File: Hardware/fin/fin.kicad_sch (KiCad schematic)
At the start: 0 parts

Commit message: move over old schematic
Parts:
- added C1, C3, C5: 10 nF, Capacitor_SMD:C_0603_1608Metric, symbol Device:C_Small
- added C10, C4: 1 uF, Capacitor_SMD:C_0603_1608Metric, symbol Device:C_Small
- added C11: 220 nF, Capacitor_SMD:C_0603_1608Metric, symbol Device:C_Small
- added C12, C13, C2, C6, C7, C8, C9: 100nF, Capacitor_SMD:C_0603_1608Metric, symbol Device:C_Small
- added D1, D2, D3, D4: LED, LED_SMD:LED_0603_1608Metric, symbol Device:LED
- added D5: DFLS160-7, Diode_SMD:D_PowerDI-123, symbol Device:D_Small
- added H1, H2, H3, H4: MountingHole_Pad, MountingHole:MountingHole_2.2mm_M2_Pad, symbol Mechanical:MountingHole_Pad
- added J1: USB_C_Receptacle_USB2.0_16P, Connector_USB:USB_C_Receptacle_GCT_USB4105-xx-A_16P_TopMnt_Horizontal, symbol Connector:USB_C_Receptacle_USB2.0_16P
- added J10, J11, J12, J13, J14, J15, J16, J17, J18, J6, J7, J8, J9: Conn_01x01_Pin, FinLib:SimpleThroughHole, symbol Connector:Conn_01x01_Pin
- added J2, J3: Conn_01x04_Pin, Connector_PinHeader_2.54mm:PinHeader_1x04_P2.54mm_Vertical, symbol Connector:Conn_01x04_Pin
- added J4: Conn_01x08_Pin, Connector_PinHeader_2.54mm:PinHeader_1x08_P2.54mm_Vertical, symbol Connector:Conn_01x08_Pin
- added J5: Conn_01x04_Pin, FinLib:FlexCable, symbol Connector:Conn_01x04_Pin
- added R1: 10 k, Resistor_SMD:R_0603_1608Metric, symbol Device:R_US
- added R10, R7, R8, R9: 220, Resistor_SMD:R_0603_1608Metric, symbol Device:R_Small_US
- added R11, R12, R13, R14: 1 k, Resistor_SMD:R_0603_1608Metric, symbol Device:R_US
- added R15, R16: 5.1k, Resistor_SMD:R_0603_1608Metric, symbol Device:R_Small_US
- added R2: 5K, Resistor_SMD:R_0603_1608Metric, symbol Device:R_Small_US
- added R3, R4, R5, R6: 2.5 k, Resistor_SMD:R_0603_1608Metric, symbol Device:R_US
- added SW1, SW2: SW_Push, FinLib:SW_FSM2JMTR_TEC, symbol Switch:SW_Push
- added TP1, TP2, TP3, TP4: TestPoint, Connector_PinHeader_2.54mm:PinHeader_1x01_P2.54mm_Vertical, symbol Connector:TestPoint
- added TP10, TP11, TP12, TP13, TP14, TP15, TP16, TP17, TP18, TP19, TP20, TP21, TP22, TP23, TP24, TP25, TP9: TestPoint, FinLib:TestPoint, symbol Connector:TestPoint
- added TP5, TP6, TP7, TP8: TestPoint, Connector_PinSocket_2.54mm:PinSocket_1x01_P2.54mm_Vertical, symbol Connector:TestPoint
- added U1: ADS131M03QPWRQ1, FinLib:ADS131M03, symbol FinLib:ADS131M03QPWRQ1
- added U2: STM32L412C8Tx, Package_QFP:LQFP-48_7x7mm_P0.5mm, symbol MCU_ST_STM32L4:STM32L412C8Tx
- added U3: W25N512GVEIG, FinLib:WSON8_8x6_E_WIN, symbol FinLib:W25N512GVEIG
- added U4: TMP235A4DBZR, FinLib:TMP235A4DBZR, symbol FinLib:TMP235A4DBZR
- added U5: FT232RNQ-REEL, FinLib:QFN32_FT232_FTD, symbol FinLib:FT232RNQ-REEL
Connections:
- new net: D4.1 (K), R10.2
- new net: R2.2, SW2.2, U2.44 (PH3)
- new net: C2.2, SW1.2, U2.7 (NRST)
- new net: D3.1 (K), R9.2
- new net: D5.2 (A), J1.A4 (VBUS), J1.A9 (VBUS), J1.B4 (VBUS), J1.B9 (VBUS)
- new net: D1.1 (K), R7.1
- new net: D2.1 (K), R8.2
- new net: C5.1, R5.2, U1.7 (AIN2P)
- new net: C5.2, R6.1, U1.8 (AIN2N)
- new net: J1.A5 (CC1), R15.1
- new net: C1.1, R1.2, U1.3 (AIN0P)
- new net: C13.1, U5.16 (3V3OUT)
- new net: C3.1, R3.2, U1.5 (AIN1N)
- new net: C3.2, R4.1, U1.6 (AIN1P)
- new net: J1.B5 (CC2), R16.1
- new net: C11.1, U1.18 (CAP)
- new net +3.3V: C10.1, C12.1, C4.2, C6.1, C7.1, C8.1, C9.1, D1.2 (A), D2.2 (A), D3.2 (A), J2.1 (Pin_1), J3.1 (Pin_1), J4.7 (Pin_7), J5.1 (Pin_1), R11.2, R13.1, SW2.1, U1.1 (AVDD), U1.20 (DVDD), U2.1 (VBAT), U2.24 (VDD), U2.48 (VDD), U2.9 (VDDA), U3.8 (VCC), U4.1 (VDD), U5.1 (VCCIO)
- new net +5V: D5.1 (K), U5.19 (VCC)
- new net ADC_~{SYNC}/~{RST}: TP14.1, U1.11 (*SYNC/*RESET), U2.46 (PB9)
- new net AVBAY_SYNC: J5.3 (Pin_3), U2.22 (PB11)
- new net GAUGE1_IN_N: R11.1, R12.1, R5.1
- new net GAUGE1_IN_P: J2.2 (Pin_2), J2.3 (Pin_3), R6.2
- new net GAUGE2_IN_N: R13.2, R14.2, R4.2
- new net GAUGE2_IN_P: J3.2 (Pin_2), J3.3 (Pin_3), R3.1
- new net GND: C1.2, C10.2, C11.2, C12.2, C13.2, C2.1, C4.1, C6.2, C7.2, C8.2, C9.2, H1.1, H2.1, H3.1, H4.1, J1.A1 (GND), J1.A12 (GND), J1.B1 (GND), J1.B12 (GND), J2.4 (Pin_4), J3.4 (Pin_4), J4.8 (Pin_8), J5.4 (Pin_4), R10.1, R12.2, R14.1, R15.2, R16.2, R2.1, R7.2, SW1.1, TP1.1, TP2.1, TP3.1, TP4.1, TP5.1, TP6.1, TP7.1, TP8.1, U1.19 (DGND), U1.2 (AGND), U1.4 (AIN0N), U2.23 (VSS), U2.35 (VSS), U2.47 (VSS), U2.8 (VSSA), U3.4 (GND), U3.9 (EPAD), U4.3 (GND), U5.17 (GND), U5.20 (GND), U5.24 (AGND), U5.26 (TEST), U5.33 (EPAD), U5.4 (GND)
- new net PA15: J8.1 (Pin_1), U2.38 (PA15)
- new net PA5: J6.1 (Pin_1), U2.15 (PA5)
- new net PA8: J7.1 (Pin_1), U2.29 (PA8)
- new net PB2: J9.1 (Pin_1), U2.20 (PB2)
- new net PB3: J10.1 (Pin_1), U2.39 (PB3)
- new net PB4: J11.1 (Pin_1), U2.40 (PB4)
- new net PB6: J12.1 (Pin_1), U2.42 (PB6)
- new net PB7: J13.1 (Pin_1), U2.43 (PB7)
- new net PC13: J14.1 (Pin_1), U2.2 (PC13)
- new net PC14: J15.1 (Pin_1), U2.3 (PC14)
- new net PC15: J16.1 (Pin_1), U2.4 (PC15)
- new net PH0: J17.1 (Pin_1), U2.5 (PH0)
- new net PH1: J18.1 (Pin_1), U2.6 (PH1)
- new net QSPI_IO0: TP17.1, U2.19 (PB1), U3.5 (DI_(IO0))
- new net QSPI_IO1: TP18.1, U2.18 (PB0), U3.2 (DO_(IO1))
- new net QSPI_IO2: TP19.1, U2.17 (PA7), U3.3 (/WP_(IO2))
- new net QSPI_IO3: TP20.1, U2.16 (PA6), U3.7 (/HOLD_(IO3))
- new net QSPI_SCK: TP16.1, U2.13 (PA3), U3.6 (CLK)
- new net SIGNAL: J5.2 (Pin_2), U2.21 (PB10)
- new net SPI1_MISO: J4.1 (Pin_1), U2.32 (PA11)
- new net SPI1_MOSI: J4.2 (Pin_2), U2.33 (PA12)
- new net SPI1_SCK: J4.6 (Pin_6), U2.11 (PA1)
- new net SPI2_MISO: TP10.1, U1.15 (DOUT), U2.27 (PB14)
- new net SPI2_MOSI: TP11.1, U1.16 (DIN), U2.28 (PB15)
- new net SPI2_SCK: TP9.1, U1.14 (SCLK), U2.26 (PB13)
- new net STATUS_LED: D4.2 (A), U2.41 (PB5)
- new net SWCLK: J4.4 (Pin_4), U2.37 (PA14)
- new net SWDIO: J4.3 (Pin_3), U2.34 (PA13)
- new net TIM2_CH1: TP13.1, U1.17 (CLKIN), U2.10 (PA0)
- new net TMP_IN_P: R1.1, U4.2 (VOUT)
- new net USART1_RX: TP22.1, U2.31 (PA10), U5.30 (TXD)
- new net USART1_TX: TP23.1, U2.30 (PA9), U5.2 (RXD)
- new net USB_D+: J1.A6 (D+), J1.B6 (D+), TP24.1, U5.14 (USBDP)
- new net USB_D-: J1.A7 (D-), J1.B7 (D-), TP25.1, U5.15 (USBDM)
- new net ~{ADC_CS}: TP12.1, U1.12 (*CS), U2.25 (PB12)
- new net ~{ADC_DRDY}: TP15.1, U1.13 (*DRDY), U2.45 (PB8)
- new net ~{FLASH_CS}: TP21.1, U2.12 (PA2), U3.1 (/CS)
- new net ~{RX_LED}: R9.1, U5.21 (CBUS1)
- new net ~{SPI1_CS}: J4.5 (Pin_5), U2.14 (PA4)
- new net ~{TX_LED}: R8.1, U5.22 (CBUS0)
- no-connect marks 0 -> 16
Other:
- note added: "ADC"
- note added: "AvBay"
- note added: "External Connections"
- note added: "Extra MCU Pins"
- note added: "Flash"
- note added: "LEDs"
- note added: "Programming/Postflight Data"
- note added: "STM32L4"
- note added: "Sensing"
- note added: "Strain Gauges"
- note added: "Test Points"
- note added: "USB"

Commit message: place fin components
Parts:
- removed C13: 100nF, Capacitor_SMD:C_0603_1608Metric, symbol Device:C_Small
- removed D2, D3: LED, LED_SMD:LED_0603_1608Metric, symbol Device:LED
- removed D5: DFLS160-7, Diode_SMD:D_PowerDI-123, symbol Device:D_Small
- removed H1, H2, H3, H4: MountingHole_Pad, MountingHole:MountingHole_2.2mm_M2_Pad, symbol Mechanical:MountingHole_Pad
- removed J1: USB_C_Receptacle_USB2.0_16P, Connector_USB:USB_C_Receptacle_GCT_USB4105-xx-A_16P_TopMnt_Horizontal, symbol Connector:USB_C_Receptacle_USB2.0_16P
- removed J10, J11, J12, J13, J14, J15, J16, J17, J18, J6, J7, J8, J9: Conn_01x01_Pin, FinLib:SimpleThroughHole, symbol Connector:Conn_01x01_Pin
- removed J4: Conn_01x08_Pin, Connector_PinHeader_2.54mm:PinHeader_1x08_P2.54mm_Vertical, symbol Connector:Conn_01x08_Pin
- removed R15, R16: 5.1k, Resistor_SMD:R_0603_1608Metric, symbol Device:R_Small_US
- removed R8, R9: 220, Resistor_SMD:R_0603_1608Metric, symbol Device:R_Small_US
- removed SW1, SW2: SW_Push, FinLib:SW_FSM2JMTR_TEC, symbol Switch:SW_Push
- removed TP1, TP2, TP3, TP4: TestPoint, Connector_PinHeader_2.54mm:PinHeader_1x01_P2.54mm_Vertical, symbol Connector:TestPoint
- removed TP10, TP11, TP12, TP13, TP14, TP15, TP16, TP17, TP18, TP19, TP20, TP21, TP22, TP23, TP24, TP25, TP9: TestPoint, FinLib:TestPoint, symbol Connector:TestPoint
- removed TP5, TP6, TP7, TP8: TestPoint, Connector_PinSocket_2.54mm:PinSocket_1x01_P2.54mm_Vertical, symbol Connector:TestPoint
- removed U5: FT232RNQ-REEL, FinLib:QFN32_FT232_FTD, symbol FinLib:FT232RNQ-REEL
- added J1: Conn_01x10_Pin, Connector_PinHeader_2.54mm:PinHeader_1x10_P2.54mm_Vertical, symbol Connector:Conn_01x10_Pin
- J5: footprint FinLib:FlexCable -> Connector_PinHeader_2.54mm:PinHeader_1x04_P2.54mm_Vertical
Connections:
- net +3.3V: now also J1.9 (Pin_9)
- net GND: now also J1.10 (Pin_10)
- net QSPI_IO0: now also J1.2 (Pin_2)
- net QSPI_IO1: now also J1.3 (Pin_3)
- net QSPI_IO2: now also J1.4 (Pin_4)
- net QSPI_IO3: now also J1.5 (Pin_5)
- net QSPI_SCK: now also J1.1 (Pin_1)
- net SWCLK: now also J1.8 (Pin_8)
- net SWDIO: now also J1.7 (Pin_7)
- net ~{FLASH_CS}: now also J1.6 (Pin_6)
- net PA15: no longer names the net of U2.38 (PA15)
- net PA5: no longer names the net of U2.15 (PA5)
- net PA8: no longer names the net of U2.29 (PA8)
- net PB2: no longer names the net of U2.20 (PB2)
- net PB3: no longer names the net of U2.39 (PB3)
- net PB4: no longer names the net of U2.40 (PB4)
- net PB6: no longer names the net of U2.42 (PB6)
- net PB7: no longer names the net of U2.43 (PB7)
- net PC13: no longer names the net of U2.2 (PC13)
- net PC14: no longer names the net of U2.3 (PC14)
- net PC15: no longer names the net of U2.4 (PC15)
- net PH0: no longer names the net of U2.5 (PH0)
- net PH1: no longer names the net of U2.6 (PH1)
- net SPI1_MISO: no longer names the net of U2.32 (PA11)
- net SPI1_MOSI: no longer names the net of U2.33 (PA12)
- net SPI1_SCK: no longer names the net of U2.11 (PA1)
- net ~{SPI1_CS}: no longer names the net of U2.14 (PA4)
- no-connect marks 16 -> 1
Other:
- note removed: "Extra MCU Pins"
- note removed: "Test Points"
- note removed: "USB"
- moved on the sheet: R2

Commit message: really scuffed draft
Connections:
- net QSPI_IO1: now also J1.4 (Pin_4); no longer J1.3 (Pin_3)
- net QSPI_IO2: now also J1.3 (Pin_3); no longer J1.4 (Pin_4)
- net SWCLK: now also J1.7 (Pin_7); no longer J1.8 (Pin_8)
- net SWDIO: now also J1.8 (Pin_8); no longer J1.7 (Pin_7)

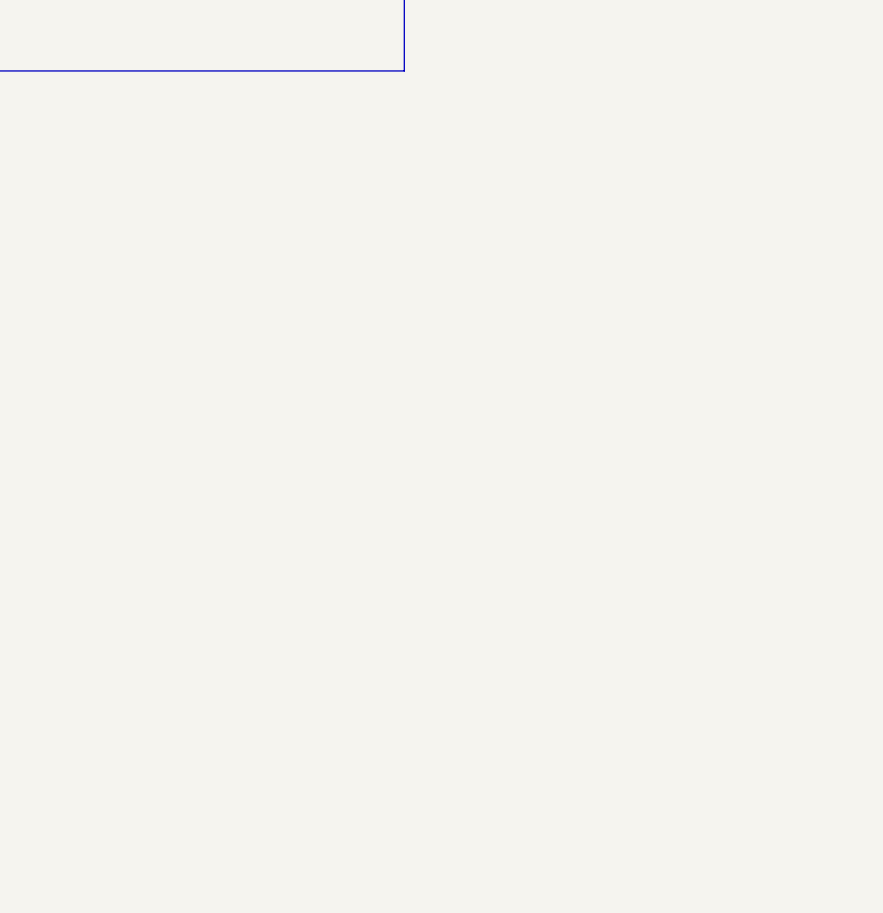
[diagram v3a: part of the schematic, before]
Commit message: add symbol for smaller STM32L412
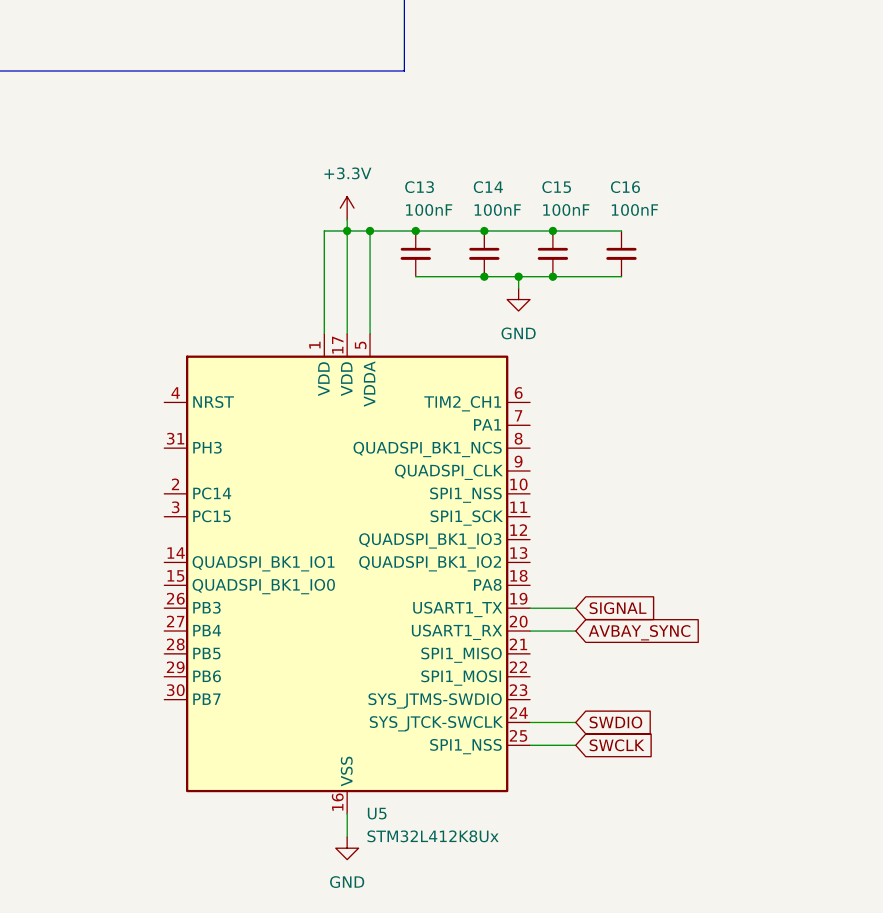
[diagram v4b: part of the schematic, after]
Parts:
- added C13, C14, C15, C16: 100nF, Capacitor_SMD:C_0603_1608Metric, symbol Device:C_Small
- added U5: STM32L412K8Ux, Package_DFN_QFN:QFN-32-1EP_5x5mm_P0.5mm_EP3.45x3.45mm, symbol MCU_ST_STM32L4:STM32L412K8Ux
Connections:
- net +3.3V: now also C13.1, C14.1, C15.1, C16.1, U5.1 (VDD), U5.17 (VDD), U5.5 (VDDA)
- net AVBAY_SYNC: now also U5.20 (PA10)
- net GND: now also C13.2, C14.2, C15.2, C16.2, U5.16 (VSS), U5.32 (VSS), U5.33 (VSS)
- net SIGNAL: now also U5.19 (PA9)
- net SWCLK: now also U5.25 (PA15)
- net SWDIO: now also U5.24 (PA14)

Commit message: updated fin schem
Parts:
- removed C6, C7, C8, C9: 100nF, Capacitor_SMD:C_0603_1608Metric, symbol Device:C_Small
- removed U2: STM32L412C8Tx, Package_QFP:LQFP-48_7x7mm_P0.5mm, symbol MCU_ST_STM32L4:STM32L412C8Tx
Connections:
- net ADC_~{SYNC}/~{RST}: now also U5.27 (PB4)
- net QSPI_IO0: now also U5.15 (PB1)
- net QSPI_IO1: now also U5.14 (PB0)
- net QSPI_IO2: now also U5.13 (PA7)
- net QSPI_IO3: now also U5.12 (PA6)
- net QSPI_SCK: now also U5.9 (PA3)
- net STATUS_LED: now also U5.28 (PB5)
- net SWCLK: now also U5.24 (PA14); no longer U5.25 (PA15)
- net SWDIO: now also U5.23 (PA13); no longer U5.24 (PA14)
- net TIM2_CH1: now also U5.6 (PA0)
- net ~{ADC_CS}: now also U5.10 (PA4)
- net ~{ADC_DRDY}: now also U5.26 (PB3)
- net ~{FLASH_CS}: now also U5.8 (PA2)
- net SPI1_SCK: now reaches U5.11 (PA5)
- net SPI1_MISO: now reaches U5.21 (PA11)
- net SPI1_MOSI: now reaches U5.22 (PA12)
- net at U5.31 (PH3): now also R2.2
- net at U5.4 (NRST): now also C2.2
- no-connect marks 1 -> 0
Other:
- moved on the sheet: C13, C14, C15, C16, C2, R2, U5

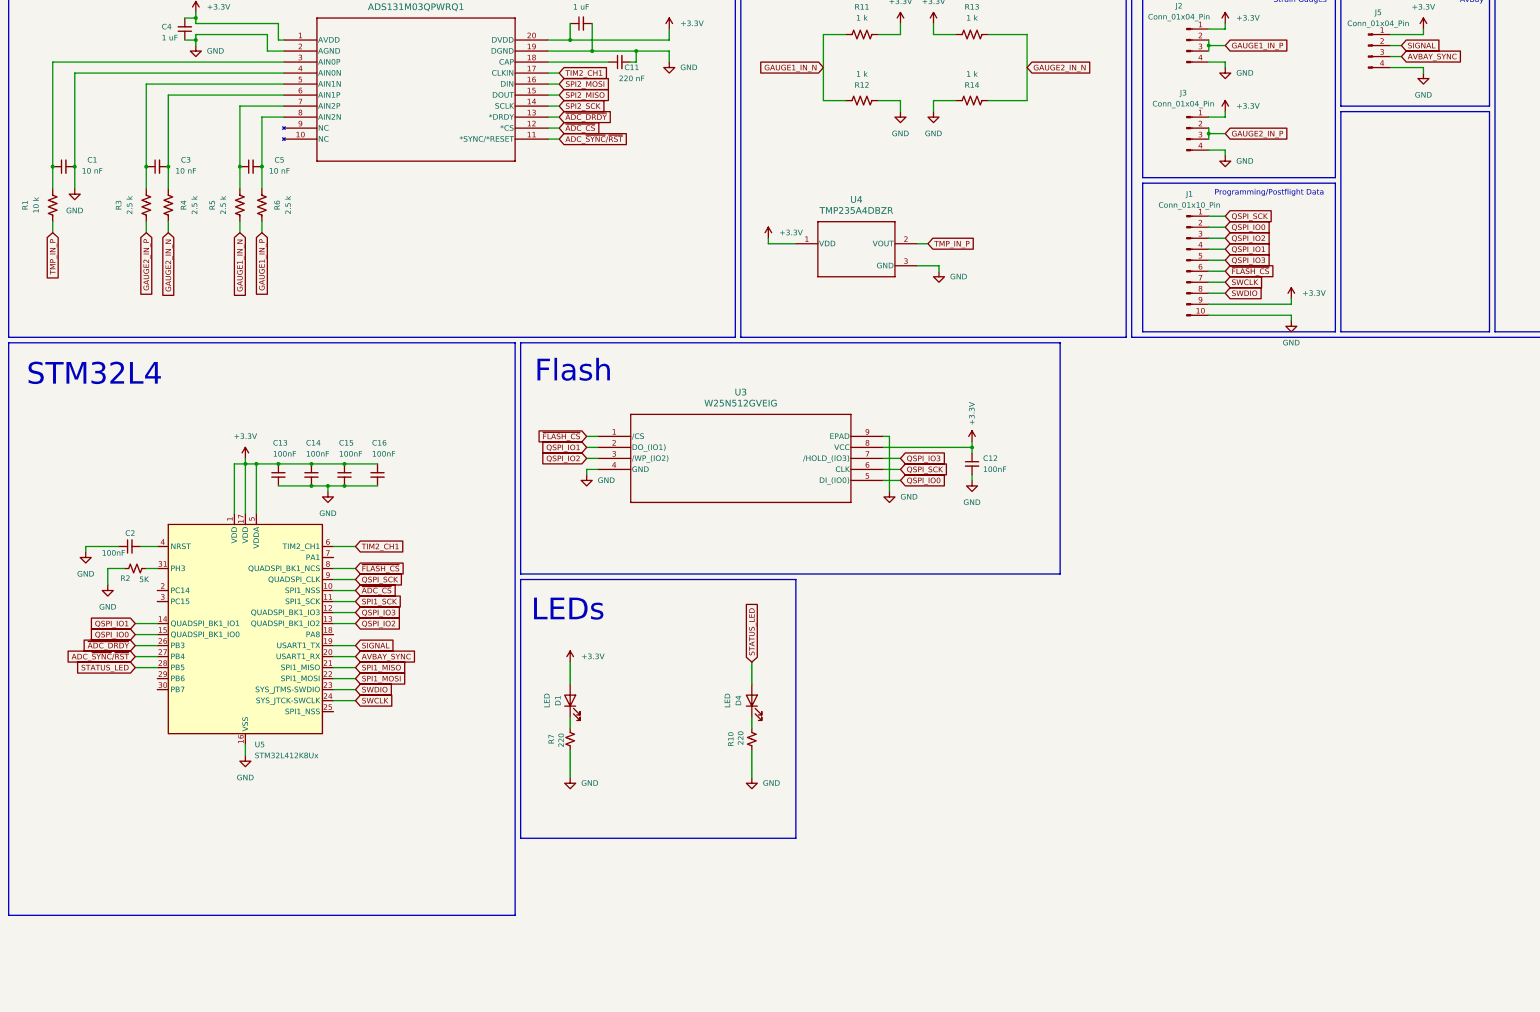
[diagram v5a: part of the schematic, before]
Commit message: accelerometers, coupled flash layout
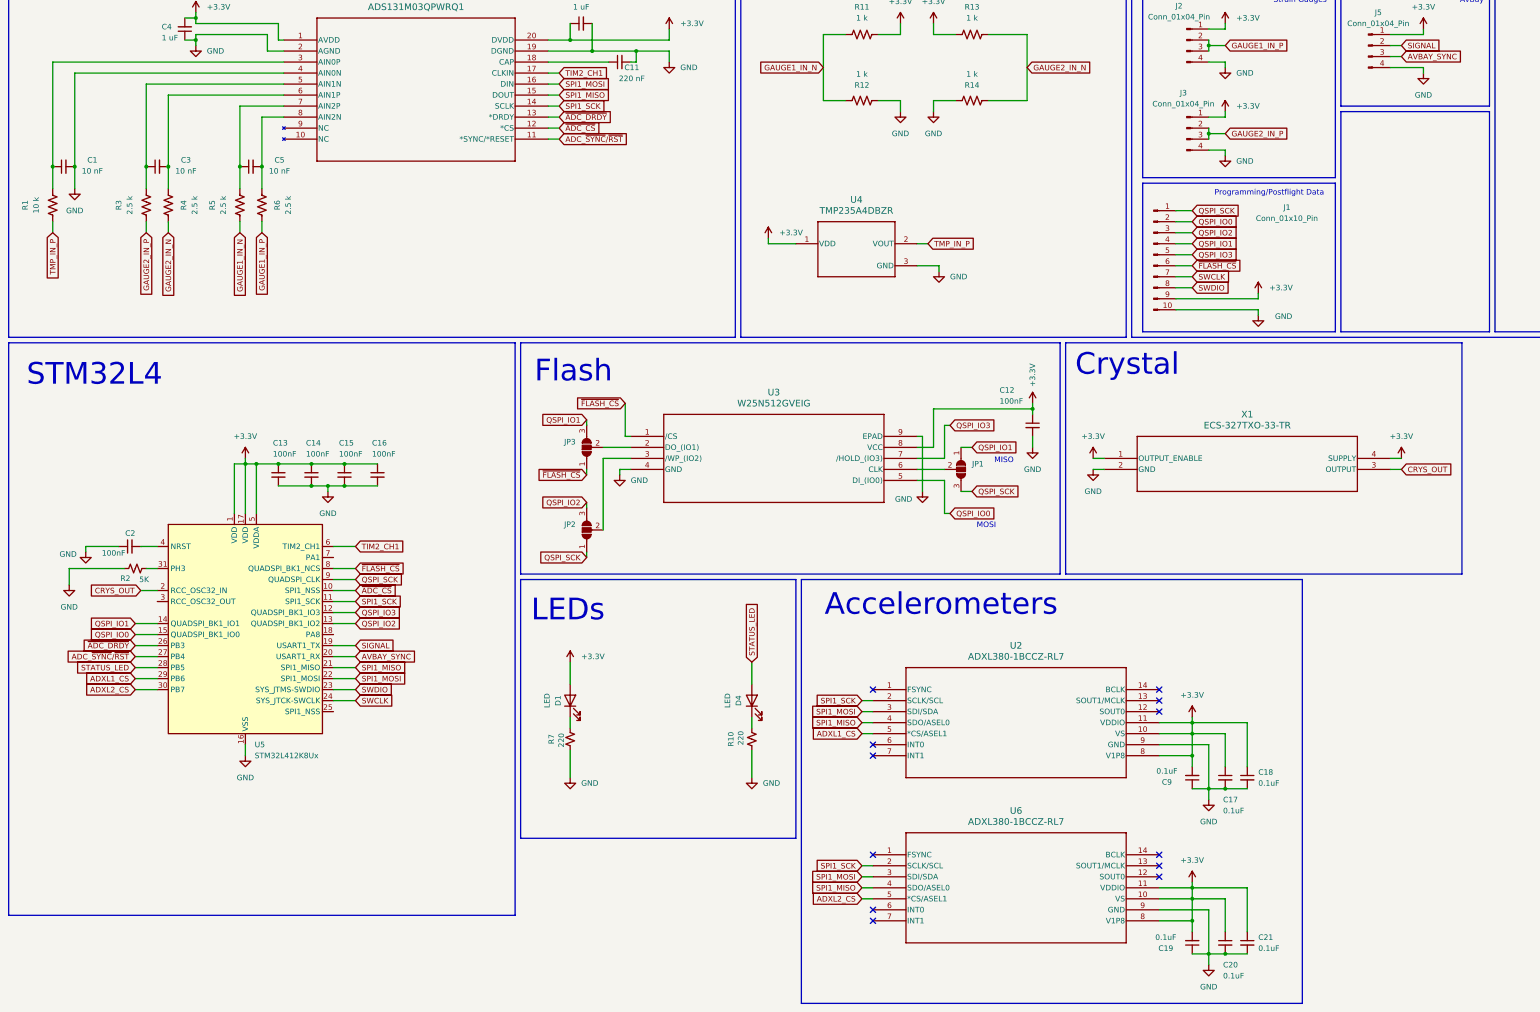
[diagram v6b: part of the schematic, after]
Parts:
- added C17, C18, C19, C20, C21, C9: 0.1uF, Capacitor_SMD:C_0603_1608Metric, symbol Device:C_Small
- added JP1, JP2, JP3: SolderJumper_3_Open, Jumper:SolderJumper-3_P1.3mm_Open_RoundedPad1.0x1.5mm, symbol Jumper:SolderJumper_3_Open
- added U2, U6: ADXL380-1BCCZ-RL7, FinLib:CC-14-3_ADI, symbol FinLib:ADXL380-1BCCZ-RL7
- added X1: ECS-327TXO-33-TR, FinLib:ECS-327_ECS, symbol FinLib:ECS-327TXO-33-TR
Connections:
- net SPI2_MISO is gone; now on net SPI1_MISO: U1.15 (DOUT)
- net SPI2_MOSI is gone; now on net SPI1_MOSI: U1.16 (DIN)
- net SPI2_SCK is gone; now on net SPI1_SCK: U1.14 (SCLK)
- net +3.3V: now also C17.1, C18.1, C19.2, C20.1, C21.1, C9.2, U2.10 (VS), U2.11 (VDDIO), U2.8 (V1P8), U6.10 (VS), U6.11 (VDDIO), U6.8 (V1P8), X1.1 (OUTPUT_ENABLE), X1.4 (SUPPLY)
- net GND: now also C17.2, C18.2, C19.1, C20.2, C21.2, C9.1, U2.9 (GND), U6.9 (GND), X1.2 (GND)
- net QSPI_IO1: now also JP1.1 (A), JP3.3 (B); no longer U3.2 (DO_(IO1))
- net QSPI_IO2: now also JP2.3 (B); no longer U3.3 (/WP_(IO2))
- net QSPI_SCK: now also JP1.3 (B), JP2.1 (A); no longer U3.6 (CLK)
- net SPI1_MISO: now also U2.4 (SDO/ASEL0), U6.4 (SDO/ASEL0)
- net SPI1_MOSI: now also U2.3 (SDI/SDA), U6.3 (SDI/SDA)
- net SPI1_SCK: now also U2.2 (SCLK/SCL), U6.2 (SCLK/SCL)
- net ~{FLASH_CS}: now also JP3.1 (A)
- net CRYS_OUT: now reaches U5.2 (PC14)
- net CRYS_OUT: now also X1.3 (OUTPUT)
- net ADXL1_CS: now reaches U5.29 (PB6)
- net ADXL1_CS: now also U2.5 (*CS/ASEL1)
- net ADXL2_CS: now reaches U5.30 (PB7)
- net ADXL2_CS: now also U6.5 (*CS/ASEL1)
- new net: JP1.2 (C), U3.6 (CLK)
- new net: JP3.2 (C), U3.2 (DO_(IO1))
- new net: JP2.2 (C), U3.3 (/WP_(IO2))
- no-connect marks 0 -> 12
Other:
- note added: "Accelerometers"
- note added: "Crystal"
- note added: "MISO"
- note added: "MOSI"
- moved on the sheet: C12, J1, U3
